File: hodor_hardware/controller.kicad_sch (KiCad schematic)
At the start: 56 parts, among them J12 Conn_01x24_Pin, J13 Conn_01x24_Socket, J4 USB_C_Receptacle_USB2.0_16P, J9 Conn_01x04_Pin, SW1 SW_RST, SW2 SW_BOOT, T21 SCL, T24 SDA, U1 ESP32-S3-WROOM-1_N8R2, U15 TPS2116DRL, U17 SSD1306, U2 TLV62569DBV, U6 MAX811SEUS-T, U9 24LC256

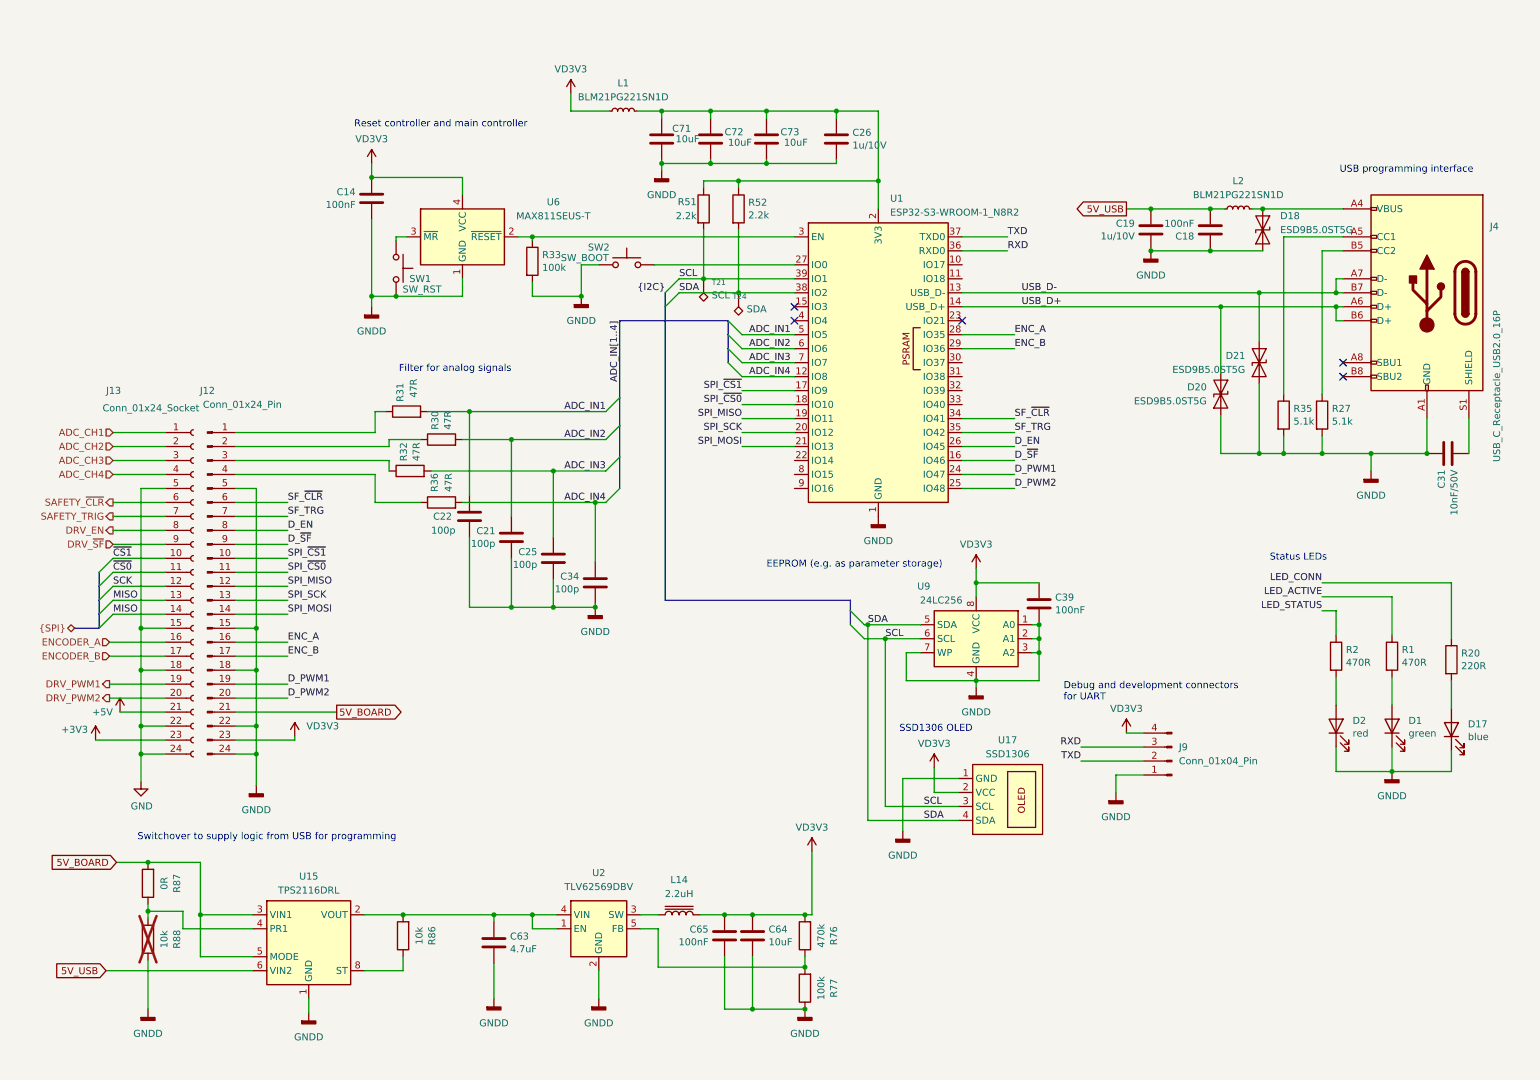
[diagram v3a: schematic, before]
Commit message: Finished schematic and initial placement on PCB
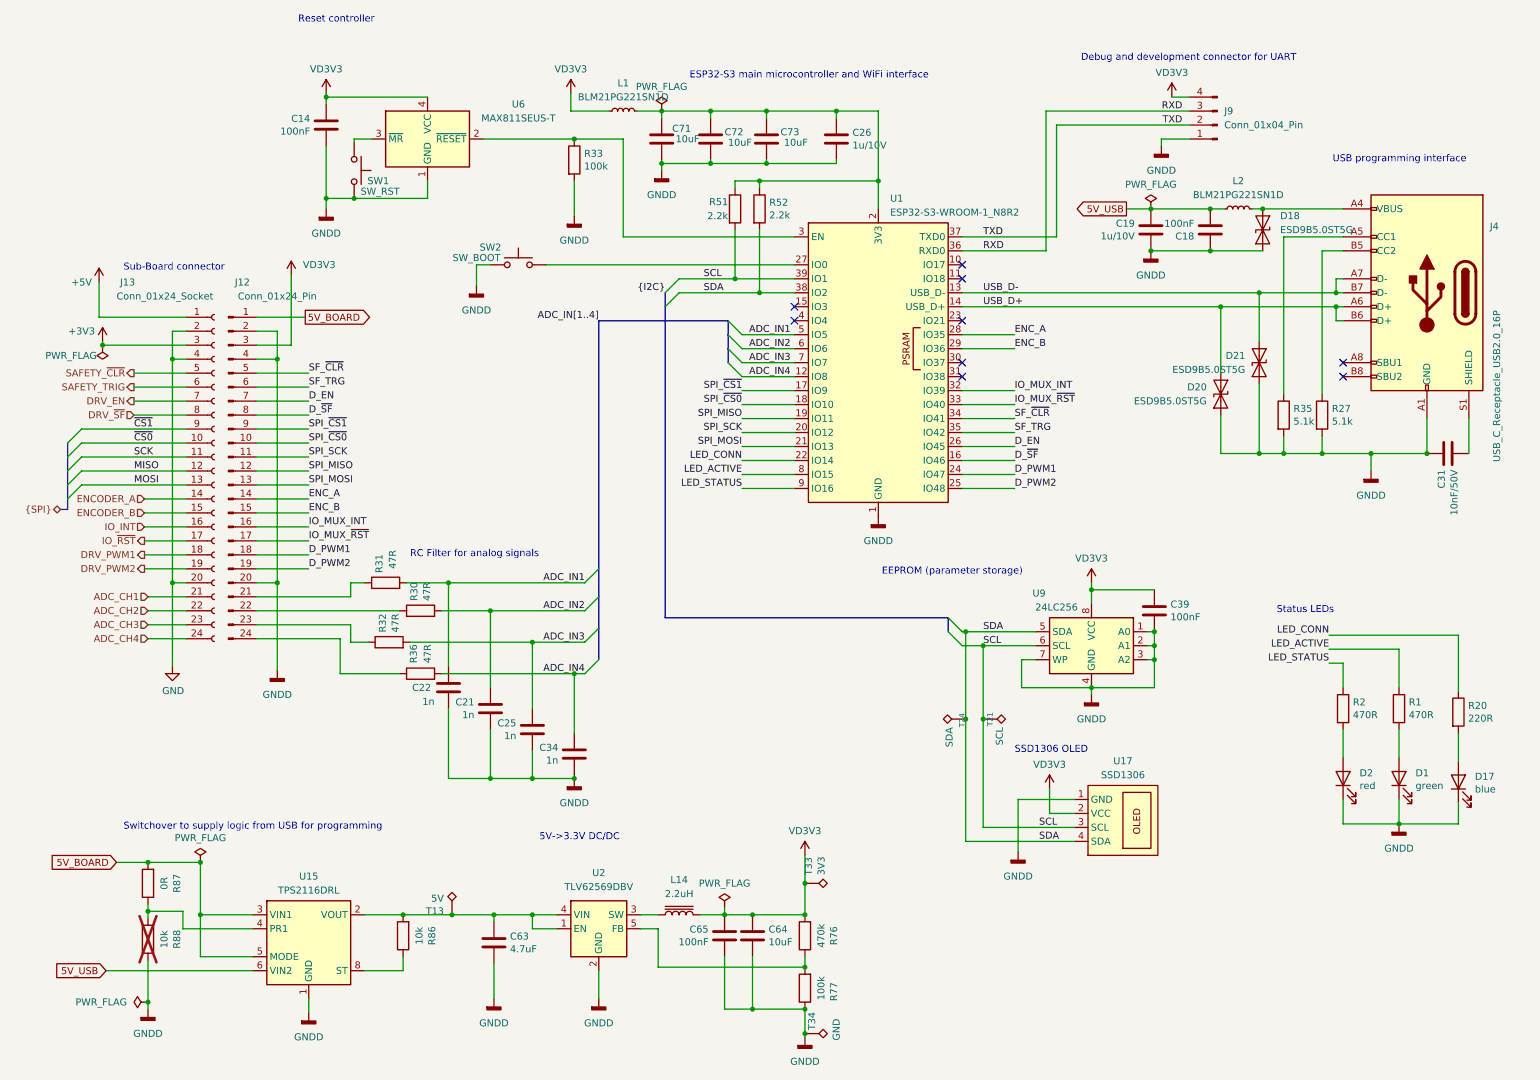
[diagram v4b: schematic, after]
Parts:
- added T13: 5V, TestPoint:TestPoint_Pad_D1.0mm, symbol Connector:TestPoint_Alt
- added T33: 3V3, TestPoint:TestPoint_Pad_D1.0mm, symbol Connector:TestPoint_Alt
- added T34: GND, TestPoint:TestPoint_Pad_1.0x1.0mm, symbol Connector:TestPoint_Alt
- C21, C22, C25, C34: value 100p -> 1n
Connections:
- net +3V3: now also J13.3 (Pin_3); no longer J13.23 (Pin_23)
- net +5V: now also J13.1 (Pin_1); no longer J13.21 (Pin_21)
- net 5V_BOARD: now also J12.1 (Pin_1); no longer J12.21 (Pin_21)
- net ADC_CH1: now also J13.21 (Pin_21); no longer J13.1 (Pin_1)
- net ADC_CH2: now also J13.22 (Pin_22); no longer J13.2 (Pin_2)
- net ADC_CH3: now also J13.23 (Pin_23); no longer J13.3 (Pin_3)
- net ADC_CH4: now also J13.24 (Pin_24); no longer J13.4 (Pin_4)
- net DRV_EN: now also J13.7 (Pin_7); no longer J13.8 (Pin_8)
- net DRV_PWM1: now also J13.18 (Pin_18); no longer J13.19 (Pin_19)
- net DRV_PWM2: now also J13.19 (Pin_19); no longer J13.20 (Pin_20)
- net DRV_~{SF}: now also J13.8 (Pin_8); no longer J13.9 (Pin_9)
- net D_EN: now also J12.7 (Pin_7); no longer J12.8 (Pin_8)
- net D_PWM1: now also J12.18 (Pin_18); no longer J12.19 (Pin_19)
- net D_PWM2: now also J12.19 (Pin_19); no longer J12.20 (Pin_20)
- net D_~{SF}: now also J12.8 (Pin_8); no longer J12.9 (Pin_9)
- net ENCODER_A: now also J13.14 (Pin_14); no longer J13.16 (Pin_16)
- net ENCODER_B: now also J13.15 (Pin_15); no longer J13.17 (Pin_17)
- net ENC_A: now also J12.14 (Pin_14); no longer J12.16 (Pin_16)
- net ENC_B: now also J12.15 (Pin_15); no longer J12.17 (Pin_17)
- net GND: now also J13.2 (Pin_2), J13.20 (Pin_20), J13.4 (Pin_4); no longer J13.15 (Pin_15), J13.18 (Pin_18), J13.22 (Pin_22), J13.24 (Pin_24), J13.5 (Pin_5)
- net GNDD: now also J12.2 (Pin_2), J12.20 (Pin_20), J12.4 (Pin_4), T34.1; no longer J12.15 (Pin_15), J12.18 (Pin_18), J12.22 (Pin_22), J12.24 (Pin_24), J12.5 (Pin_5)
- net LED_ACTIVE: now also U1.8 (IO15)
- net LED_CONN: now also U1.22 (IO14)
- net LED_STATUS: now also U1.9 (IO16)
- net MISO: now also J13.12 (Pin_12); no longer J13.13 (Pin_13), J13.14 (Pin_14)
- net SAFETY_TRIG: now also J13.6 (Pin_6); no longer J13.7 (Pin_7)
- net SAFETY_~{CLR}: now also J13.5 (Pin_5); no longer J13.6 (Pin_6)
- net SCK: now also J13.11 (Pin_11); no longer J13.12 (Pin_12)
- net SF_TRG: now also J12.6 (Pin_6); no longer J12.7 (Pin_7)
- net SF_~{CLR}: now also J12.5 (Pin_5); no longer J12.6 (Pin_6)
- net SPI_MOSI: now also J12.13 (Pin_13); no longer J12.14 (Pin_14)
- net SPI_SCK: now also J12.11 (Pin_11); no longer J12.13 (Pin_13)
- net SPI_~{CS0}: now also J12.10 (Pin_10); no longer J12.11 (Pin_11)
- net SPI_~{CS1}: now also J12.9 (Pin_9); no longer J12.10 (Pin_10)
- net VD3V3: now also J12.3 (Pin_3), T33.1; no longer J12.23 (Pin_23)
- net ~{CS0}: now also J13.10 (Pin_10); no longer J13.11 (Pin_11)
- net ~{CS1}: now also J13.9 (Pin_9); no longer J13.10 (Pin_10)
- net at R31.1: now also J12.21 (Pin_21); no longer J12.1 (Pin_1)
- net at R30.1: now also J12.22 (Pin_22); no longer J12.2 (Pin_2)
- net at R32.1: now also J12.23 (Pin_23); no longer J12.3 (Pin_3)
- net at R36.1: now also J12.24 (Pin_24); no longer J12.4 (Pin_4)
- net at C63.1, R86.2, U15.2 (VOUT)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: now also T13.1
- net IO_MUX_INT: now reaches U1.32 (IO39)
- net IO_MUX_INT: now also J12.16 (Pin_16)
- net IO_MUX_~{RST}: now reaches U1.33 (IO40)
- net IO_MUX_~{RST}: now also J12.17 (Pin_17)
- new net IO_INT: J13.16 (Pin_16)
- new net IO_~{RST}: J13.17 (Pin_17)
- new net MOSI: J13.13 (Pin_13)
- no-connect marks 5 -> 9
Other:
- note added: "5V->3.3V DC/DC"
- note added: "Debug and development connector for UART"
- note added: "EEPROM (parameter storage)"
- note added: "ESP32-S3 main microcontroller and WiFi interface"
- note added: "RC Filter for analog signals"
- note added: "Reset controller"
- note added: "Sub-Board connector"
- note removed: "Debug and development connectors for UART"
- note removed: "EEPROM (e.g. as parameter storage)"
- note removed: "Filter for analog signals"
- note removed: "Reset controller and main controller"
- moved on the sheet: C14, C21, C22, C25, C34, C39, D1, D17, D2, J12, J13, J9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

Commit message: Latest changes
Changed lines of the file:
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@@
 	(text "Reset controller"
 		(exclude_from_sim no)
-		(at 64.135 8.89 0)
+		(at 66.04 15.875 0)
 		(effects
 			(font
